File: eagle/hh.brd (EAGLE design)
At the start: 169.7 x 51.9 mm, 6 parts

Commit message: wiring 1
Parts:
- turned JP1 to 270 degrees
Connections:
- new net GND: U$1.GND@3
- new net N$1: U$1.3V3@2
- new net N$3: JP1.1, U$1.3V3@1
- new net N$4: JP1.2, U$1.GND@2
- new net N$5: JP1.3, U$1.D1
- new net N$6: JP1.4, U$1.D2
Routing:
- net N$3: track 0.00 -> 138.1 mm, vias 0 -> 1
- net N$4: track 0.00 -> 109.7 mm, vias 0 -> 1
- net N$6: track 0.00 -> 71.4 mm
- net N$5: track 0.00 -> 64.5 mm
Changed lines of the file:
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@@
 </element>
 <element name="U$1" library="ESP12E_DEVKIT" package="ESP12E_DEVKIT" value="ESP12E_DEVKIT" x="27.53" y="35.83" rot="R270"/>
-<element name="JP1" library="pinhead" package="1X04" value="OLED" x="91.02" y="37.75" rot="R90"/>
+<element name="JP1" library="pinhead" package="1X04" value="OLED" x="91.02" y="37.75" rot="R270"/>
 </elements>
 <signals>
-<signal name="N$2">
+<signal name="GND">
+<contactref element="U$1" pad="GND@3"/>
+</signal>
+<signal name="N$1">
+<contactref element="U$1" pad="3V3@2"/>
+</signal>
+<signal name="N$3">
+<contactref element="JP1" pad="1"/>
+<contactref element="U$1" pad="3V3@1"/>
+<wire x1="91.02" y1="41.56" x2="33" y2="41" width="0.4064" layer="16"/>
+<wire x1="33" y1="41" x2="32.61" y2="24.4" width="0.4064" layer="16"/>
+<via x="90.9" y="19.05" extent="1-16" drill="1.6" shape="square"/>
+<wire x1="90.7542" y1="18.9738" x2="90.9" y2="19.05" width="0.254" layer="1"/>
+<wire x1="90.9" y1="19.05" x2="33" y2="19" width="0.4064" layer="16"/>
+<wire x1="33" y1="19" x2="32.61" y2="24.4" width="0.4064" layer="16"/>
+</signal>
+<signal name="N$4">
+<contactref element="JP1" pad="2"/>
+<contactref element="U$1" pad="GND@2"/>
+<wire x1="91.02" y1="39.02" x2="95" y2="39" width="0.4064" layer="16"/>
+<wire x1="95" y1="39" x2="95" y2="44" width="0.4064" layer="16"/>
+<wire x1="95" y1="44" x2="30" y2="44" width="0.4064" layer="16"/>
+<wire x1="30" y1="44" x2="30.07" y2="24.4" width="0.4064" layer="16"/>
 <via x="19.4" y="19.05" extent="1-16" drill="1.6" shape="square"/>
-<via x="90.9" y="19.05" extent="1-16" drill="1.6" shape="square"/>
+<wire x1="19.431" y1="18.9738" x2="19.4" y2="19.05" width="0.254" layer="1"/>
+<wire x1="19.4" y1="19.05" x2="30" y2="19" width="0.4064" layer="16"/>
+<wire x1="30" y1="19" x2="30.07" y2="24.4" width="0.4064" layer="16"/>
+</signal>
+<signal name="N$6">
+<contactref element="JP1" pad="4"/>
+<contactref element="U$1" pad="D2"/>
+<wire x1="91.02" y1="33.94" x2="93" y2="34" width="0.4064" layer="1"/>
+<wire x1="93" y1="34" x2="93" y2="21" width="0.4064" layer="1"/>
+<wire x1="93" y1="21" x2="40" y2="21" width="0.4064" layer="1"/>
+<wire x1="40" y1="21" x2="40.23" y2="24.4" width="0.4064" layer="1"/>
+</signal>
+<signal name="N$5">
+<contactref element="JP1" pad="3"/>
+<contactref element="U$1" pad="D1"/>
+<wire x1="91.02" y1="36.48" x2="89" y2="36" width="0.4064" layer="1"/>
+<wire x1="89" y1="36" x2="89" y2="22" width="0.4064" layer="1"/>
+<wire x1="89" y1="22" x2="43" y2="22" width="0.4064" layer="1"/>
+<wire x1="43" y1="22" x2="42.77" y2="24.4" width="0.4064" layer="1"/>
 </signal>
 </signals>

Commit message: wiring 2
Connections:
- new net N$2: S4.1, S4.2, U$1.D3
- new net N$7: S3.1, S3.2, U$1.D4
- new net N$8: S2.1, S2.2, U$1.D5
- new net N$9: S1.1, S1.2, U$1.D6
- net GND: now also S1.3, S1.4, S2.3, S2.4, S3.3, S3.4, S4.3, S4.4
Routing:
- net GND: track 0.00 -> 113.6 mm
- net N$2: track 0.00 -> 52.0 mm
- net N$7: track 0.00 -> 42.0 mm
- net N$8: track 0.00 -> 37.0 mm
- net N$9: track 0.00 -> 28.0 mm
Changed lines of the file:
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@@
 <signal name="GND">
 <contactref element="U$1" pad="GND@3"/>
+<contactref element="S4" pad="3"/>
+<contactref element="S3" pad="3"/>
+<contactref element="S2" pad="3"/>
+<contactref element="S1" pad="3"/>
+<contactref element="S1" pad="4"/>
+<contactref element="S2" pad="4"/>
+<contactref element="S3" pad="4"/>
+<contactref element="S4" pad="4"/>
+<wire x1="12.29" y1="24.4" x2="12" y2="5" width="0.4064" layer="16"/>
+<wire x1="12" y1="5" x2="29.3194" y2="5.4488" width="0.4064" layer="16"/>
+<wire x1="29.3194" y1="5.4488" x2="29" y2="2" width="0.4064" layer="16"/>
+<wire x1="29" y1="2" x2="42" y2="2" width="0.4064" layer="16"/>
+<wire x1="41.8994" y1="5.4488" x2="42" y2="2" width="0.4064" layer="16"/>
+<wire x1="42" y1="2" x2="54" y2="2" width="0.4064" layer="16"/>
+<wire x1="54" y1="2" x2="53.4794" y2="5.4488" width="0.4064" layer="16"/>
+<wire x1="54" y1="2" x2="66" y2="2" width="0.4064" layer="16"/>
+<wire x1="66" y1="2" x2="66.0594" y2="5.4488" width="0.4064" layer="16"/>
+<wire x1="29.3194" y1="5.4488" x2="29.3194" y2="11.9512" width="0.4064" layer="16"/>
+<wire x1="41.8994" y1="5.4488" x2="41.8994" y2="11.9512" width="0.4064" layer="16"/>
+<wire x1="53.4794" y1="5.4488" x2="53.4794" y2="11.9512" width="0.4064" layer="16"/>
+<wire x1="66.0594" y1="5.4488" x2="66.0594" y2="11.9512" width="0.4064" layer="16"/>
 </signal>
 <signal name="N$1">
@@
 <wire x1="43" y1="22" x2="42.77" y2="24.4" width="0.4064" layer="1"/>
 </signal>
+<signal name="N$2">
+<contactref element="U$1" pad="D3"/>
+<contactref element="S4" pad="2"/>
+<contactref element="S4" pad="1"/>
+<wire x1="37.69" y1="24.4" x2="38" y2="19" width="0.4064" layer="1"/>
+<wire x1="38" y1="19" x2="71" y2="19" width="0.4064" layer="1"/>
+<wire x1="71" y1="19" x2="70.5806" y2="11.9512" width="0.4064" layer="1"/>
+<wire x1="70.5806" y1="11.9512" x2="70.5806" y2="5.4488" width="0.4064" layer="1"/>
+</signal>
+<signal name="N$7">
+<contactref element="U$1" pad="D4"/>
+<contactref element="S3" pad="2"/>
+<contactref element="S3" pad="1"/>
+<wire x1="35.15" y1="24.4" x2="35" y2="18" width="0.4064" layer="1"/>
+<wire x1="35" y1="18" x2="58" y2="18" width="0.4064" layer="1"/>
+<wire x1="58" y1="18" x2="58.0006" y2="11.9512" width="0.4064" layer="1"/>
+<wire x1="58.0006" y1="11.9512" x2="58.0006" y2="5.4488" width="0.4064" layer="1"/>
+</signal>
+<signal name="N$8">
+<contactref element="U$1" pad="D5"/>
+<contactref element="S2" pad="2"/>
+<contactref element="S2" pad="1"/>
+<wire x1="27.53" y1="24.4" x2="28" y2="17" width="0.4064" layer="1"/>
+<wire x1="28" y1="17" x2="28" y2="16" width="0.4064" layer="1"/>
+<wire x1="28" y1="16" x2="46" y2="16" width="0.4064" layer="1"/>
+<wire x1="46" y1="16" x2="46.4206" y2="11.9512" width="0.4064" layer="1"/>
+<wire x1="46.4206" y1="11.9512" x2="46.4206" y2="5.4488" width="0.4064" layer="1"/>
+</signal>
+<signal name="N$9">
+<contactref element="U$1" pad="D6"/>
+<contactref element="S1" pad="2"/>
+<contactref element="S1" pad="1"/>
+<wire x1="24.99" y1="24.4" x2="25" y2="15" width="0.4064" layer="1"/>
+<wire x1="25" y1="15" x2="34" y2="15" width="0.4064" layer="1"/>
+<wire x1="34" y1="15" x2="33.8406" y2="11.9512" width="0.4064" layer="1"/>
+<wire x1="33.8406" y1="11.9512" x2="33.8406" y2="5.4488" width="0.4064" layer="1"/>
+</signal>
 </signals>

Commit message: fix eagle drc error
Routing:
- net N$4: track 109.7 -> 121.6 mm
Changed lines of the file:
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@@
 </class>
 </classes>
-<designrules name="default">
+<designrules name="osh">
 <description language="de">&lt;b&gt;EAGLE Design Rules&lt;/b&gt;
 &lt;p&gt;
@@
 Einstellungen hier und speichern die Design Rules unter
 einem neuen Namen ab.</description>
-<description language="en">&lt;b&gt;EAGLE Design Rules&lt;/b&gt;
+<description language="en">&lt;b&gt;Laen's PCB Order Design Rules&lt;/b&gt;
 &lt;p&gt;
-The default Design Rules have been set to cover
-a wide range of applications. Your particular design
-may have different requirements, so please make the
-necessary adjustments and save your customized
-design rules under a new name.</description>
+Please make sure your boards conform to these design rules.</description>
 <param name="layerSetup" value="(1*16)"/>
-<param name="mtCopper" value="0.035mm 0.035mm 0.035mm 0.035mm 0.035mm 0.035mm 0.035mm 0.035mm 0.035mm 0.035mm 0.035mm 0.035mm 0.035mm 0.035mm 0.035mm 0.035mm"/>
-<param name="mtIsolate" value="1.5mm 0.15mm 0.2mm 0.15mm 0.2mm 0.15mm 0.2mm 0.15mm 0.2mm 0.15mm 0.2mm 0.15mm 0.2mm 0.15mm 0.2mm"/>
-<param name="mdWireWire" value="8mil"/>
-<param name="mdWirePad" value="8mil"/>
-<param name="mdWireVia" value="8mil"/>
-<param name="mdPadPad" value="8mil"/>
-<param name="mdPadVia" value="8mil"/>
-<param name="mdViaVia" value="8mil"/>
-<param name="mdSmdPad" value="8mil"/>
-<param name="mdSmdVia" value="8mil"/>
-<param name="mdSmdSmd" value="8mil"/>
+<param name="mtCopper" value="0.0356mm 0.0356mm 0.0356mm 0.0356mm 0.0356mm 0.0356mm 0.0356mm 0.0356mm 0.0356mm 0.0356mm 0.0356mm 0.0356mm 0.0356mm 0.0356mm 0.0356mm 0.0356mm"/>
+<param name="mtIsolate" value="1.5011mm 0.1499mm 0.2007mm 0.1499mm 0.2007mm 0.1499mm 0.2007mm 0.1499mm 0.2007mm 0.1499mm 0.2007mm 0.1499mm 0.2007mm 0.1499mm 0.2007mm"/>
+<param name="mdWireWire" value="6mil"/>
+<param name="mdWirePad" value="6mil"/>
+<param name="mdWireVia" value="6mil"/>
+<param name="mdPadPad" value="6mil"/>
+<param name="mdPadVia" value="6mil"/>
+<param name="mdViaVia" value="6mil"/>
+<param name="mdSmdPad" value="6mil"/>
+<param name="mdSmdVia" value="6mil"/>
+<param name="mdSmdSmd" value="6mil"/>
 <param name="mdViaViaSameLayer" value="8mil"/>
 <param name="mnLayersViaInSmd" value="2"/>
-<param name="mdCopperDimension" value="40mil"/>
-<param name="mdDrill" value="8mil"/>
+<param name="mdCopperDimension" value="15mil"/>
+<param name="mdDrill" value="6mil"/>
 <param name="mdSmdStop" value="0mil"/>
-<param name="msWidth" value="10mil"/>
-<param name="msDrill" value="24mil"/>
-<param name="msMicroVia" value="9.99mm"/>
+<param name="msWidth" value="6mil"/>
+<param name="msDrill" value="13mil"/>
+<param name="msMicroVia" value="13mil"/>
 <param name="msBlindViaRatio" value="0.5"/>
 <param name="rvPadTop" value="0.25"/>
@@
 <param name="rvMicroViaOuter" value="0.25"/>
 <param name="rvMicroViaInner" value="0.25"/>
-<param name="rlMinPadTop" value="10mil"/>
+<param name="rlMinPadTop" value="7mil"/>
 <param name="rlMaxPadTop" value="20mil"/>
-<param name="rlMinPadInner" value="10mil"/>
+<param name="rlMinPadInner" value="7mil"/>
 <param name="rlMaxPadInner" value="20mil"/>
-<param name="rlMinPadBottom" value="10mil"/>
+<param name="rlMinPadBottom" value="7mil"/>
 <param name="rlMaxPadBottom" value="20mil"/>
-<param name="rlMinViaOuter" value="8mil"/>
+<param name="rlMinViaOuter" value="7mil"/>
 <param name="rlMaxViaOuter" value="20mil"/>
-<param name="rlMinViaInner" value="8mil"/>
+<param name="rlMinViaInner" value="7mil"/>
 <param name="rlMaxViaInner" value="20mil"/>
 <param name="rlMinMicroViaOuter" value="4mil"/>
@@
 <contactref element="U$1" pad="GND@2"/>
 <wire x1="91.02" y1="39.02" x2="95" y2="39" width="0.4064" layer="16"/>
-<wire x1="95" y1="39" x2="95" y2="44" width="0.4064" layer="16"/>
-<wire x1="95" y1="44" x2="30" y2="44" width="0.4064" layer="16"/>
-<wire x1="30" y1="44" x2="30.07" y2="24.4" width="0.4064" layer="16"/>
 <via x="19.4" y="19.05" extent="1-16" drill="1.6" shape="square"/>
 <wire x1="19.431" y1="18.9738" x2="19.4" y2="19.05" width="0.254" layer="1"/>
 <wire x1="19.4" y1="19.05" x2="30" y2="19" width="0.4064" layer="16"/>
 <wire x1="30" y1="19" x2="30.07" y2="24.4" width="0.4064" layer="16"/>
+<wire x1="30.07" y1="24.4" x2="31" y2="24.4" width="0.4064" layer="16"/>
+<wire x1="31" y1="24.4" x2="31" y2="43" width="0.4064" layer="16"/>
+<wire x1="31" y1="42" x2="23" y2="42" width="0" layer="19" extent="1-16"/>
+<wire x1="55" y1="50" x2="95" y2="50" width="0.4064" layer="16"/>
+<wire x1="95" y1="50" x2="95" y2="39" width="0.4064" layer="16"/>
+<wire x1="23" y1="50" x2="55" y2="50" width="0" layer="19" extent="1-16"/>
+<wire x1="55" y1="50" x2="55" y2="43" width="0.4064" layer="16"/>
+<wire x1="55" y1="43" x2="31" y2="43" width="0.4064" layer="16"/>
+<wire x1="31" y1="43" x2="31" y2="42" width="0" layer="19" extent="1-16"/>
 </signal>
 <signal name="N$6">

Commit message: testing final design
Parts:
- renumbered U$1 to ESP12E_DEVKIT
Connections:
- net N$8: now also ESP12E_DEVKIT.D0; no longer ESP12E_DEVKIT.D5
- net N$9: now also ESP12E_DEVKIT.RX; no longer ESP12E_DEVKIT.D6
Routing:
- net N$8: track 37.0 -> 20.1 mm
- net N$9: track 28.0 -> 36.0 mm
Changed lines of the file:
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@@
 <attribute name="OC_FARNELL" value="176432" x="68.32" y="8.7" size="1.778" layer="27" rot="R270" display="off"/>
 </element>
-<element name="U$1" library="ESP12E_DEVKIT" package="ESP12E_DEVKIT" value="ESP12E_DEVKIT" x="27.53" y="35.83" rot="R270"/>
+<element name="ESP12E_DEVKIT" library="ESP12E_DEVKIT" package="ESP12E_DEVKIT" value="ESP12E_DEVKIT" x="27.53" y="35.83" rot="R270"/>
 <element name="JP1" library="pinhead" package="1X04" value="OLED" x="91.02" y="37.75" rot="R270"/>
 </elements>
 <signals>
 <signal name="GND">
-<contactref element="U$1" pad="GND@3"/>
+<contactref element="ESP12E_DEVKIT" pad="GND@3"/>
 <contactref element="S4" pad="3"/>
 <contactref element="S3" pad="3"/>
@@
 </signal>
 <signal name="N$1">
-<contactref element="U$1" pad="3V3@2"/>
+<contactref element="ESP12E_DEVKIT" pad="3V3@2"/>
 </signal>
 <signal name="N$3">
 <contactref element="JP1" pad="1"/>
-<contactref element="U$1" pad="3V3@1"/>
+<contactref element="ESP12E_DEVKIT" pad="3V3@1"/>
 <wire x1="91.02" y1="41.56" x2="33" y2="41" width="0.4064" layer="16"/>
 <wire x1="33" y1="41" x2="32.61" y2="24.4" width="0.4064" layer="16"/>
@@
 <signal name="N$4">
 <contactref element="JP1" pad="2"/>
-<contactref element="U$1" pad="GND@2"/>
+<contactref element="ESP12E_DEVKIT" pad="GND@2"/>
 <wire x1="91.02" y1="39.02" x2="95" y2="39" width="0.4064" layer="16"/>
 <via x="19.4" y="19.05" extent="1-16" drill="1.6" shape="square"/>
@@
 <signal name="N$6">
 <contactref element="JP1" pad="4"/>
-<contactref element="U$1" pad="D2"/>
+<contactref element="ESP12E_DEVKIT" pad="D2"/>
 <wire x1="91.02" y1="33.94" x2="93" y2="34" width="0.4064" layer="1"/>
 <wire x1="93" y1="34" x2="93" y2="21" width="0.4064" layer="1"/>
@@
 <signal name="N$5">
 <contactref element="JP1" pad="3"/>
-<contactref element="U$1" pad="D1"/>
+<contactref element="ESP12E_DEVKIT" pad="D1"/>
 <wire x1="91.02" y1="36.48" x2="89" y2="36" width="0.4064" layer="1"/>
 <wire x1="89" y1="36" x2="89" y2="22" width="0.4064" layer="1"/>
@@
 </signal>
 <signal name="N$2">
-<contactref element="U$1" pad="D3"/>
+<contactref element="ESP12E_DEVKIT" pad="D3"/>
 <contactref element="S4" pad="2"/>
 <contactref element="S4" pad="1"/>
@@
 </signal>
 <signal name="N$7">
-<contactref element="U$1" pad="D4"/>
+<contactref element="ESP12E_DEVKIT" pad="D4"/>
 <contactref element="S3" pad="2"/>
 <contactref element="S3" pad="1"/>
@@
 </signal>
 <signal name="N$8">
-<contactref element="U$1" pad="D5"/>
 <contactref element="S2" pad="2"/>
 <contactref element="S2" pad="1"/>
-<wire x1="27.53" y1="24.4" x2="28" y2="17" width="0.4064" layer="1"/>
-<wire x1="28" y1="17" x2="28" y2="16" width="0.4064" layer="1"/>
-<wire x1="28" y1="16" x2="46" y2="16" width="0.4064" layer="1"/>
-<wire x1="46" y1="16" x2="46.4206" y2="11.9512" width="0.4064" layer="1"/>
 <wire x1="46.4206" y1="11.9512" x2="46.4206" y2="5.4488" width="0.4064" layer="1"/>
+<contactref element="ESP12E_DEVKIT" pad="D0"/>
+<wire x1="46.4206" y1="11.9512" x2="45.31" y2="11.9512" width="0.4064" layer="16"/>
+<wire x1="45.31" y1="11.9512" x2="45.31" y2="24.4" width="0.4064" layer="16"/>
 </signal>
 <signal name="N$9">
-<contactref element="U$1" pad="D6"/>
 <contactref element="S1" pad="2"/>
 <contactref element="S1" pad="1"/>
-<wire x1="24.99" y1="24.4" x2="25" y2="15" width="0.4064" layer="1"/>
-<wire x1="25" y1="15" x2="34" y2="15" width="0.4064" layer="1"/>
+<wire x1="17.37" y1="15" x2="34" y2="15" width="0.4064" layer="1"/>
 <wire x1="34" y1="15" x2="33.8406" y2="11.9512" width="0.4064" layer="1"/>
 <wire x1="33.8406" y1="11.9512" x2="33.8406" y2="5.4488" width="0.4064" layer="1"/>
+<contactref element="ESP12E_DEVKIT" pad="RX"/>
+<wire x1="17" y1="15" x2="17.37" y2="15" width="0.4064" layer="1"/>
+<wire x1="17.37" y1="15" x2="17.37" y2="24.4" width="0.4064" layer="1"/>
 </signal>
 </signals>

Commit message: tweaks
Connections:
- net N$8: now also ESP12E_DEVKIT.RX; no longer ESP12E_DEVKIT.D0
- net N$9: now also ESP12E_DEVKIT.TX; no longer ESP12E_DEVKIT.RX
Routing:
- net N$8: track 20.1 -> 49.9 mm
- net N$9: track 36.0 -> 38.5 mm
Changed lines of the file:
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@@
 <contactref element="S2" pad="1"/>
 <wire x1="46.4206" y1="11.9512" x2="46.4206" y2="5.4488" width="0.4064" layer="1"/>
-<contactref element="ESP12E_DEVKIT" pad="D0"/>
-<wire x1="46.4206" y1="11.9512" x2="45.31" y2="11.9512" width="0.4064" layer="16"/>
-<wire x1="45.31" y1="11.9512" x2="45.31" y2="24.4" width="0.4064" layer="16"/>
+<contactref element="ESP12E_DEVKIT" pad="RX"/>
+<wire x1="45.31" y1="11.9512" x2="46.4206" y2="11.9512" width="0.4064" layer="16"/>
+<wire x1="17.37" y1="24.4" x2="17" y2="24.4" width="0.4064" layer="16"/>
+<wire x1="17" y1="24.4" x2="17" y2="15" width="0.4064" layer="16"/>
+<wire x1="17" y1="15" x2="46.4206" y2="15" width="0.4064" layer="16"/>
+<wire x1="46.4206" y1="15" x2="46.4206" y2="11.9512" width="0.4064" layer="16"/>
 </signal>
 <signal name="N$9">
 <contactref element="S1" pad="2"/>
 <contactref element="S1" pad="1"/>
-<wire x1="17.37" y1="15" x2="34" y2="15" width="0.4064" layer="1"/>
 <wire x1="34" y1="15" x2="33.8406" y2="11.9512" width="0.4064" layer="1"/>
 <wire x1="33.8406" y1="11.9512" x2="33.8406" y2="5.4488" width="0.4064" layer="1"/>
-<contactref element="ESP12E_DEVKIT" pad="RX"/>
 <wire x1="17" y1="15" x2="17.37" y2="15" width="0.4064" layer="1"/>
-<wire x1="17.37" y1="15" x2="17.37" y2="24.4" width="0.4064" layer="1"/>
+<contactref element="ESP12E_DEVKIT" pad="TX"/>
+<wire x1="34" y1="15" x2="14.83" y2="15" width="0.4064" layer="1"/>
+<wire x1="14.83" y1="15" x2="14.83" y2="24.4" width="0.4064" layer="1"/>
+<wire x1="14.83" y1="15" x2="17" y2="15" width="0" layer="19" extent="1-1"/>
 </signal>
 </signals>

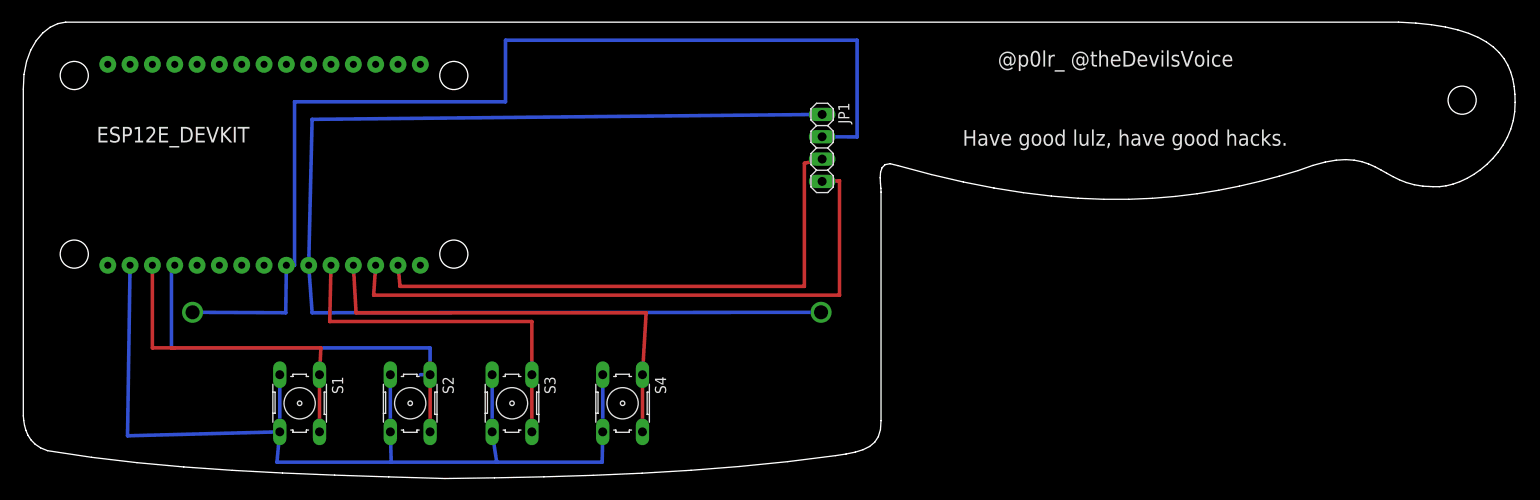
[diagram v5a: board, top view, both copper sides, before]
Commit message: Added battery clips, fixed VIN, moved switches closer together to accommodate the battery clips, added a ground plane under the radio.
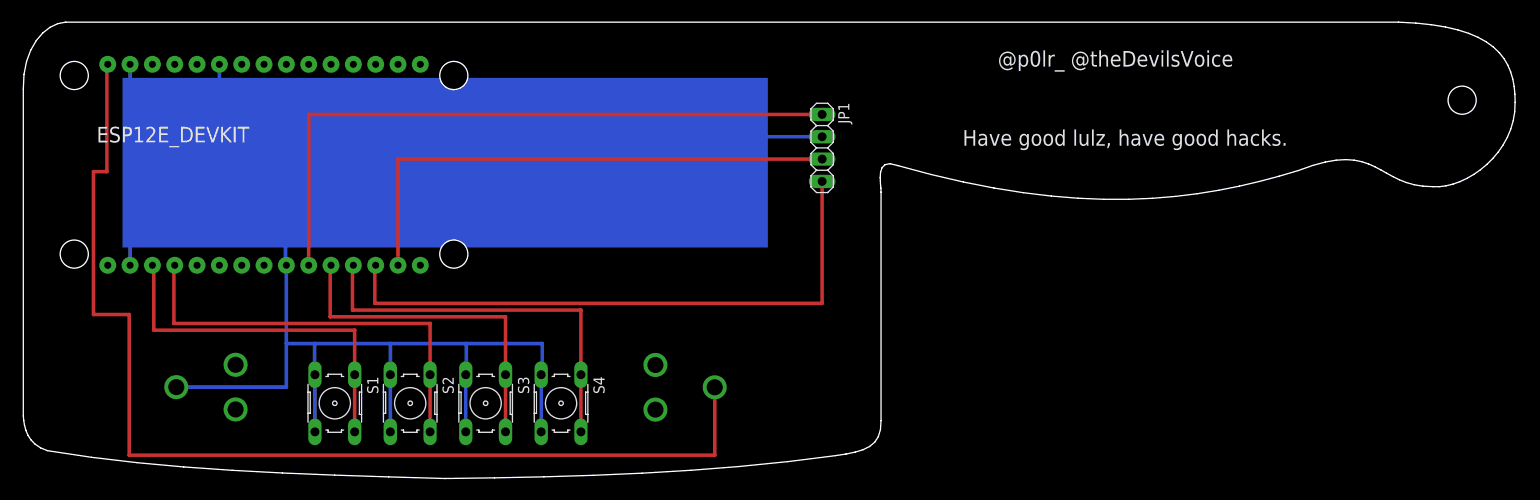
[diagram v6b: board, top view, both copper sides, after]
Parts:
- added BAT1: (no value), SparkFun-Electromechanical:BATTERY_18650-HOLDER
- moved S4 7.00 mm to (61.3, 8.70)
- moved S1 4.00 mm to (35.6, 8.70)
- moved S3 3.00 mm to (52.7, 8.70)
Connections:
- removed net GND: ESP12E_DEVKIT.GND@3, S1.3, S1.4, S2.3, S2.4, S3.3, S3.4, S4.3, S4.4
- net N$1: now also BAT1.GND@1, ESP12E_DEVKIT.GND@0, ESP12E_DEVKIT.GND@1, ESP12E_DEVKIT.GND@2, ESP12E_DEVKIT.GND@3, JP1.2, S1.3, S1.4, S2.3, S2.4, S3.3, S3.4, S4.3, S4.4; no longer ESP12E_DEVKIT.3V3@2
- net N$4: now also BAT1.PWR@1, ESP12E_DEVKIT.VIN; no longer ESP12E_DEVKIT.GND@2, JP1.2
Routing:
- net N$1: track 0.00 -> 220.5 mm
- net GND: track 113.6 -> 0.00 mm
- net N$3: track 138.1 -> 75.6 mm, vias 1 -> 0
- net N$2: track 52.0 -> 45.1 mm
- net N$5: track 64.5 -> 60.3 mm
- net N$9: track 38.5 -> 42.3 mm
- net N$4: track 121.6 -> 124.5 mm, vias 1 -> 0
- net N$7: track 42.0 -> 39.3 mm
- net N$6: track 71.4 -> 69.2 mm
- net N$8: track 49.9 -> 48.6 mm

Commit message: Add files via upload
Latest Update
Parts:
- moved S1 42.2 mm to (77.7, 7.68), turned to 90 degrees
- moved S3 35.3 mm to (88.0, 7.68), turned to 90 degrees
- moved S2 35.0 mm to (77.7, 18.9), turned to 90 degrees
- moved S4 28.5 mm to (88.0, 18.9), turned to 90 degrees
- moved BAT1 12.1 mm to (36.2, 12.6), turned to 180 degrees
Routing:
- net N$4: track 124.5 -> 50.0 mm
- net N$9: track 42.3 -> 88.2 mm
- net N$1: track 220.5 -> 262.4 mm
- net N$7: track 39.3 -> 78.2 mm
- net N$8: track 48.6 -> 74.5 mm
- net N$2: track 45.1 -> 64.7 mm
- net N$6: track 69.2 -> 64.4 mm
